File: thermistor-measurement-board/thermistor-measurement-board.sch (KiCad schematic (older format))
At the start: 0 parts

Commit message: took care of a few board review tasks
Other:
- note removed: "TODO:\nBias supplies\nOptional LDO for analog section?\nadditional (optional) bias mux footprint?\ntest points where needed"
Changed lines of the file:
@@
 Comment4 ""
 $EndDescr
-Text Notes 7000 7100 0    60   ~ 0
-TODO:\nBias supplies\nOptional LDO for analog section?\nadditional (optional) bias mux footprint?\ntest points where needed
 $Sheet
 S 6000 2100 1000 1500
@@
 $EndSheet
 $Sheet
-S 6000 3900 1000 2100
+S 6000 3900 1000 2400
 U 56B5D807
 F0 "Measurement" 60
@@
 F10 "ADC_DR_INT" I L 6000 4500 60
 F11 "ADC_RST" I L 6000 4400 60
-F12 "OUT_B+" I L 6000 5800 60
-F13 "OUT_B-" I L 6000 5900 60
+F12 "OUT_B+" I L 6000 6100 60
+F13 "OUT_B-" I L 6000 6200 60
 F14 "AMP_MUX_CS" I L 6000 5000 60
 F15 "AMP_MUX_EN" I L 6000 4900 60
-F16 "OUT_A+" I L 6000 5500 60
-F17 "OUT_A-" I L 6000 5600 60
+F16 "OUT_A+" I L 6000 5800 60
+F17 "OUT_A-" I L 6000 5900 60
 F18 "ADC_MCLK" I L 6000 4800 60
 F19 "REF_A" I L 6000 5200 60
 F20 "REF_B" I L 6000 5300 60
+F21 "ADC_REF+" I L 6000 5500 60
+F22 "ADC_REF-" I L 6000 5600 60
 $EndSheet
 $Comp
@@
 $EndComp
 $Sheet
-S 3700 3600 1400 2400
+S 3700 3600 1400 2700
 U 56B64232
 F0 "Interface" 60
@@
 F15 "ADC_DR_INT" I R 5100 4500 60
 F16 "ADC_RST" I R 5100 4400 60
-F17 "OUT_A+" I R 5100 5500 60
-F18 "OUT_A-" I R 5100 5600 60
-F19 "OUT_B+" I R 5100 5800 60
-F20 "OUT_B-" I R 5100 5900 60
+F17 "OUT_A+" I R 5100 5800 60
+F18 "OUT_A-" I R 5100 5900 60
+F19 "OUT_B+" I R 5100 6100 60
+F20 "OUT_B-" I R 5100 6200 60
 F21 "AMP_MUX_CS" O R 5100 5000 60
 F22 "AMP_MUX_EN" O R 5100 4900 60
@@
 F29 "VREF2_EN" O L 3700 5000 60
 F30 "VREF1_EN" O L 3700 4900 60
+F31 "ADC_REF+" I R 5100 5500 60
+F32 "ADC_REF-" I R 5100 5600 60
 $EndSheet
 Text Label 7500 3200 2    60   ~ 0
@@
 	5100 5300 6000 5300
 Wire Wire Line
-	6000 5500 5100 5500
-Wire Wire Line
-	5100 5600 6000 5600
+	6000 5800 5100 5800
+Wire Wire Line
+	5100 5900 6000 5900
 Wire Wire Line
 	6000 5000 5100 5000
 Wire Wire Line
-	6000 5800 5100 5800
-Wire Wire Line
-	5100 5900 6000 5900
+	6000 6100 5100 6100
+Wire Wire Line
+	5100 6200 6000 6200
 Text Label 7500 2400 2    60   ~ 0
 VS_BIAS
@@
 Wire Wire Line
 	3700 4900 3200 4900
+Wire Wire Line
+	6000 5500 5100 5500
+Wire Wire Line
+	5100 5600 6000 5600
 $EndSCHEMATC

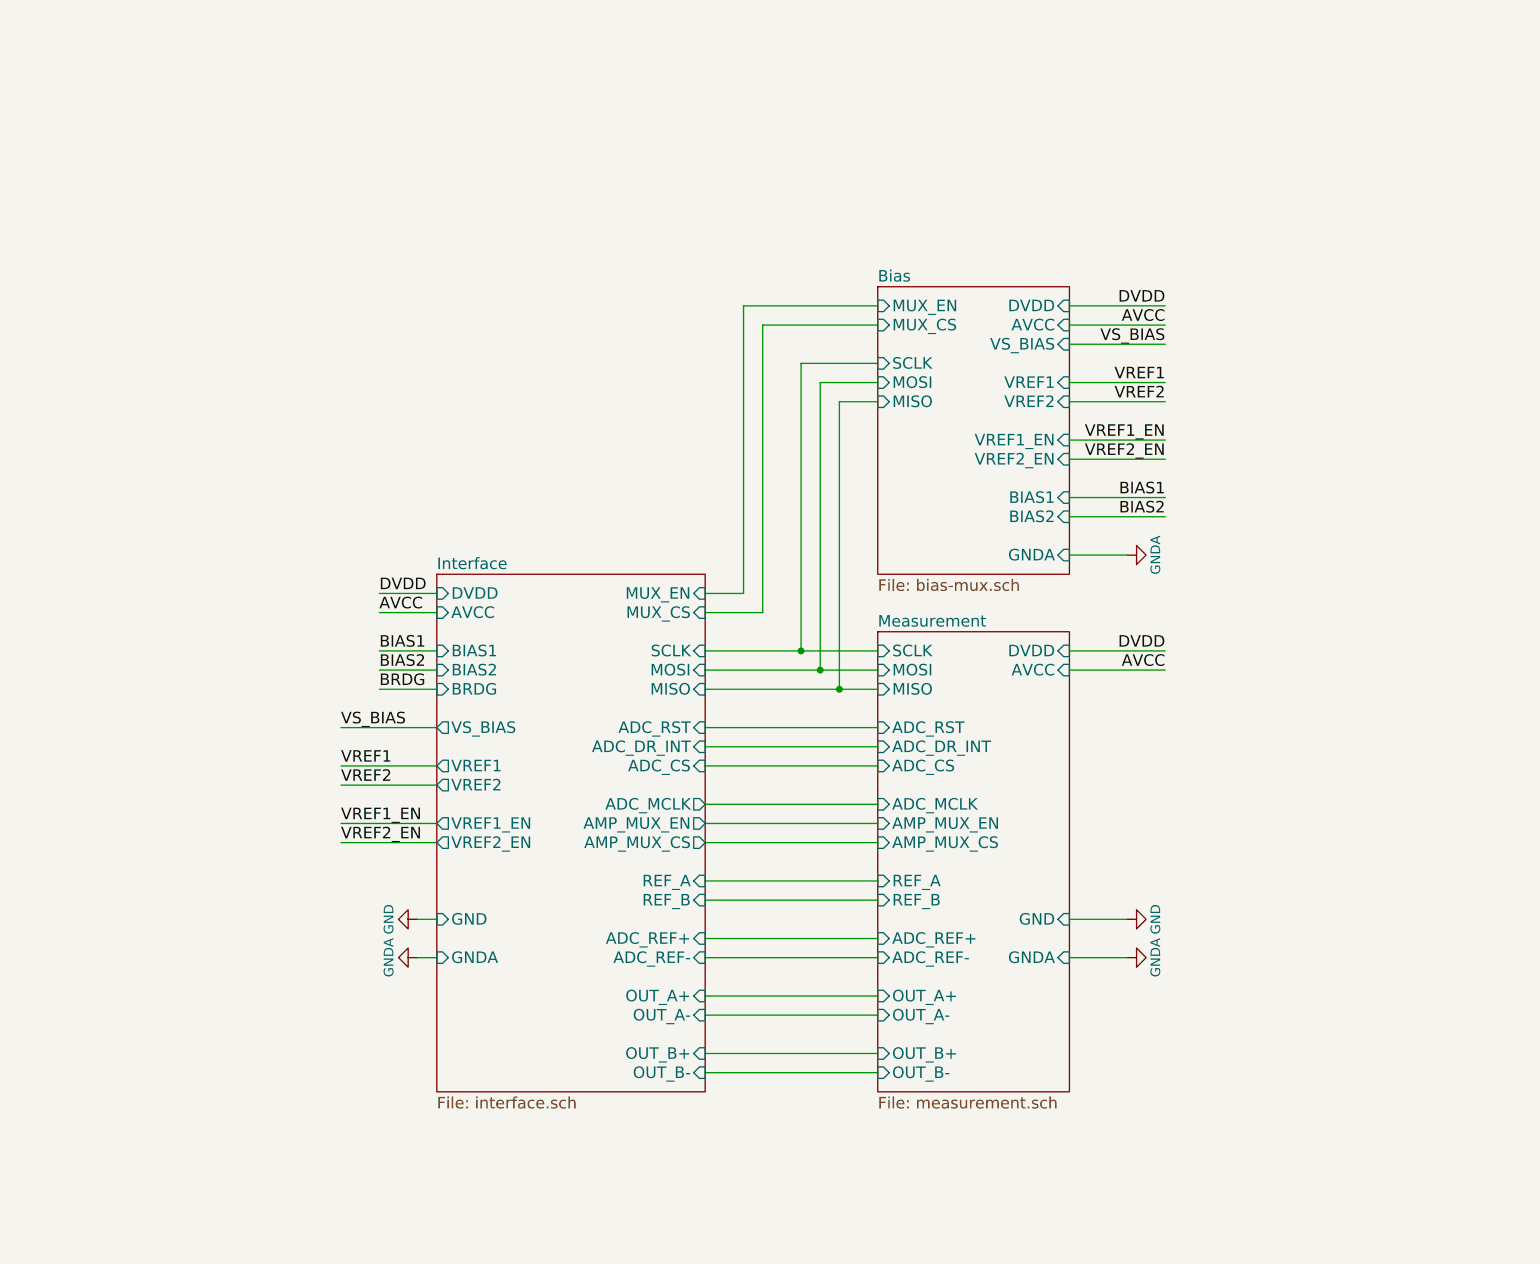
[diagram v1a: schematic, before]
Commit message: read a million instrument amp datasheets and found one that should work nicely for low gain.
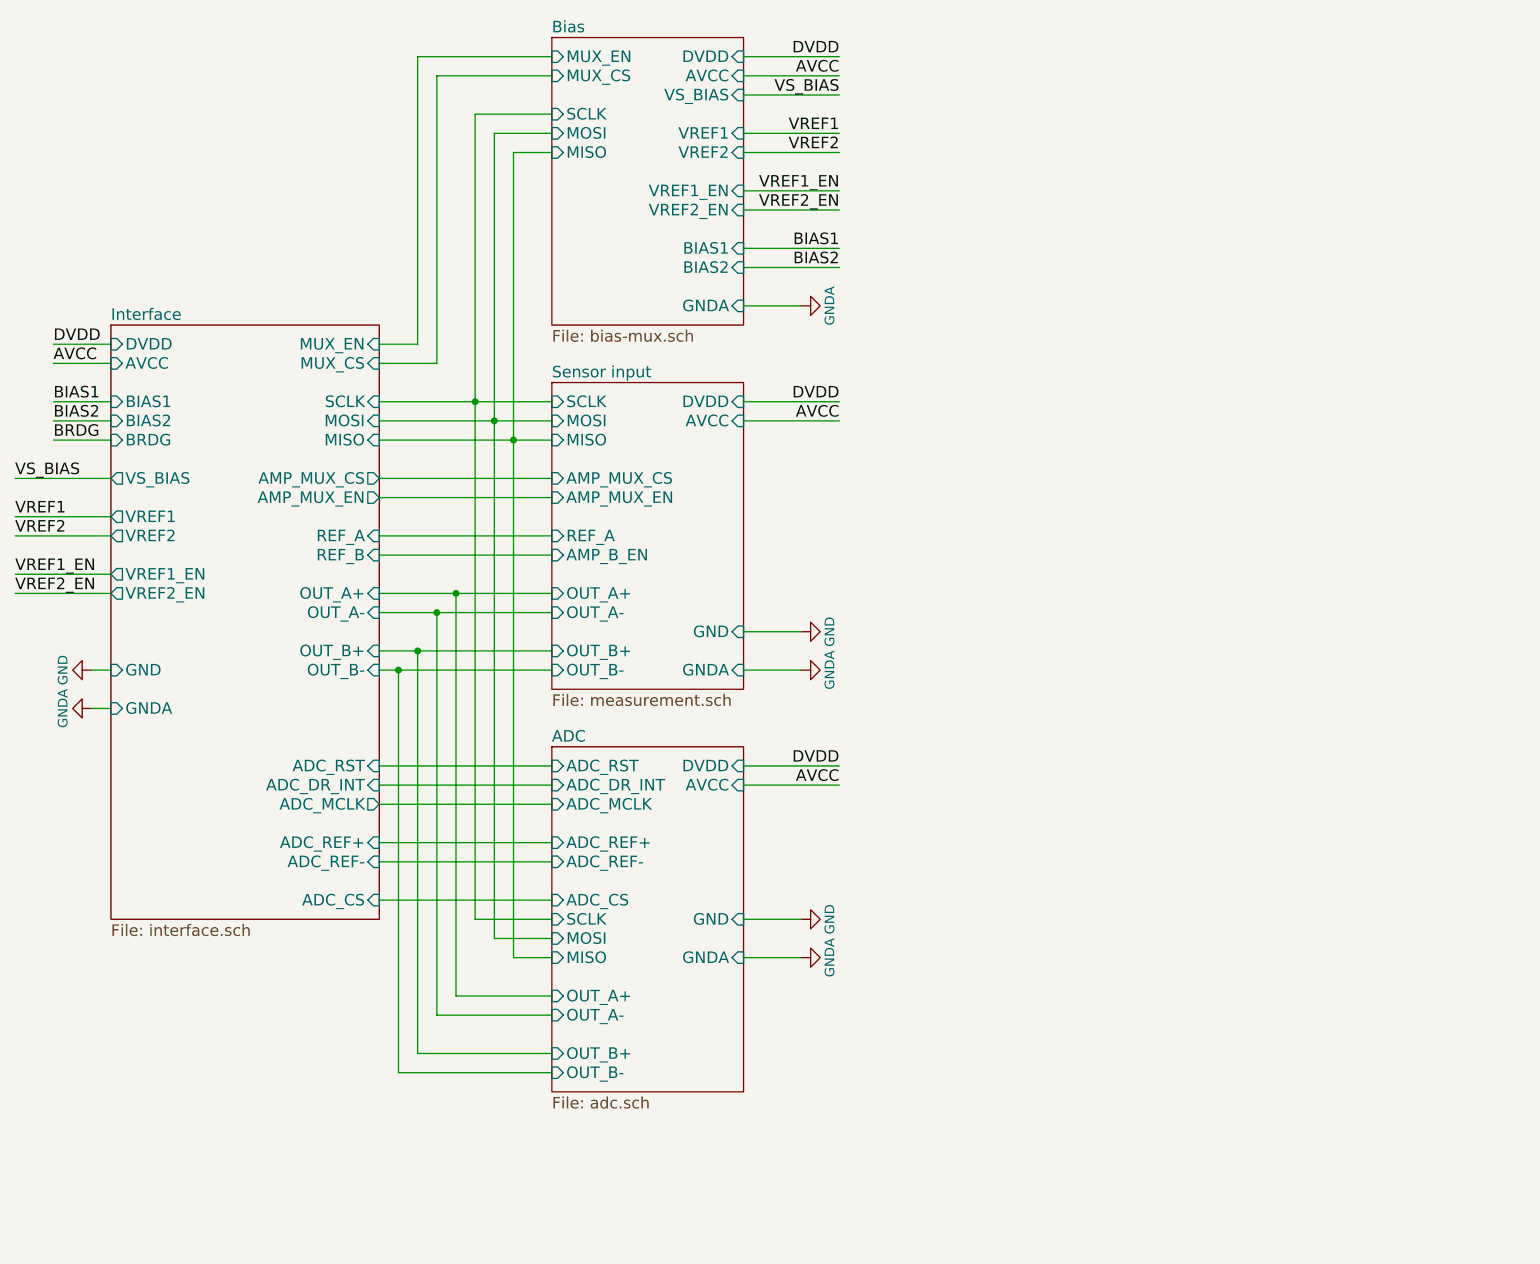
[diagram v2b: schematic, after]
